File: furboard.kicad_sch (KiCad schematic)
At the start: 28 parts, among them J1 USB_C_Receptacle_USB2.0_14P, U1 RP2040, U2 NCP1117-3.3_SOT223, U3 W25Q128JVS, Y1 12 MHz

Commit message: Update the schematic data sheet thing
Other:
- title: (none) -> Furboard Devboard Schematic
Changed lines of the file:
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@@
 	(generator_version "9.0")
 	(paper "A4")
+	(title_block
+		(title "Furboard Devboard Schematic")
+	)
 	(text_box "RP2040"
 		(exclude_from_sim no)

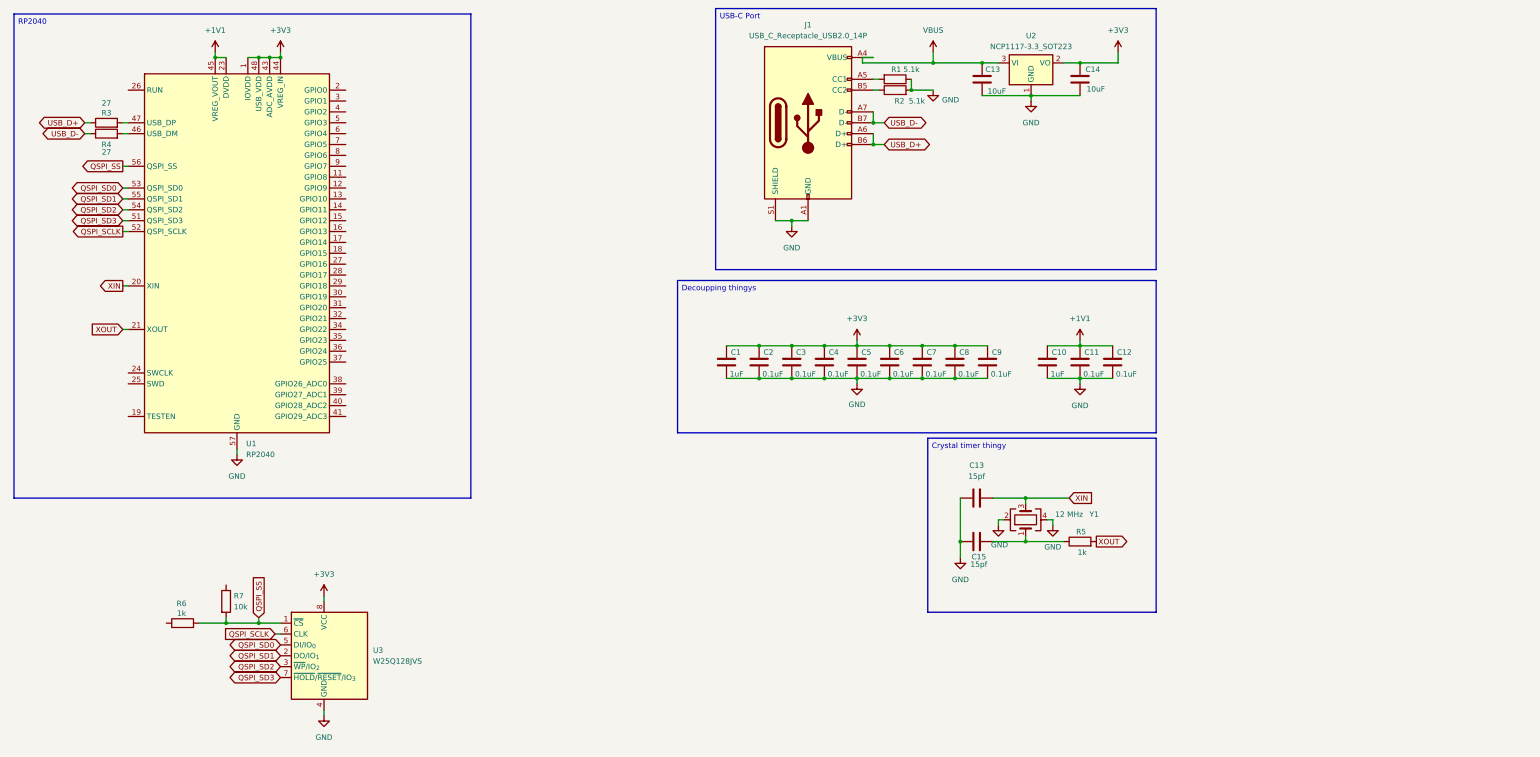
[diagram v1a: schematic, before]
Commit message: Finish schematic draft, add pinout
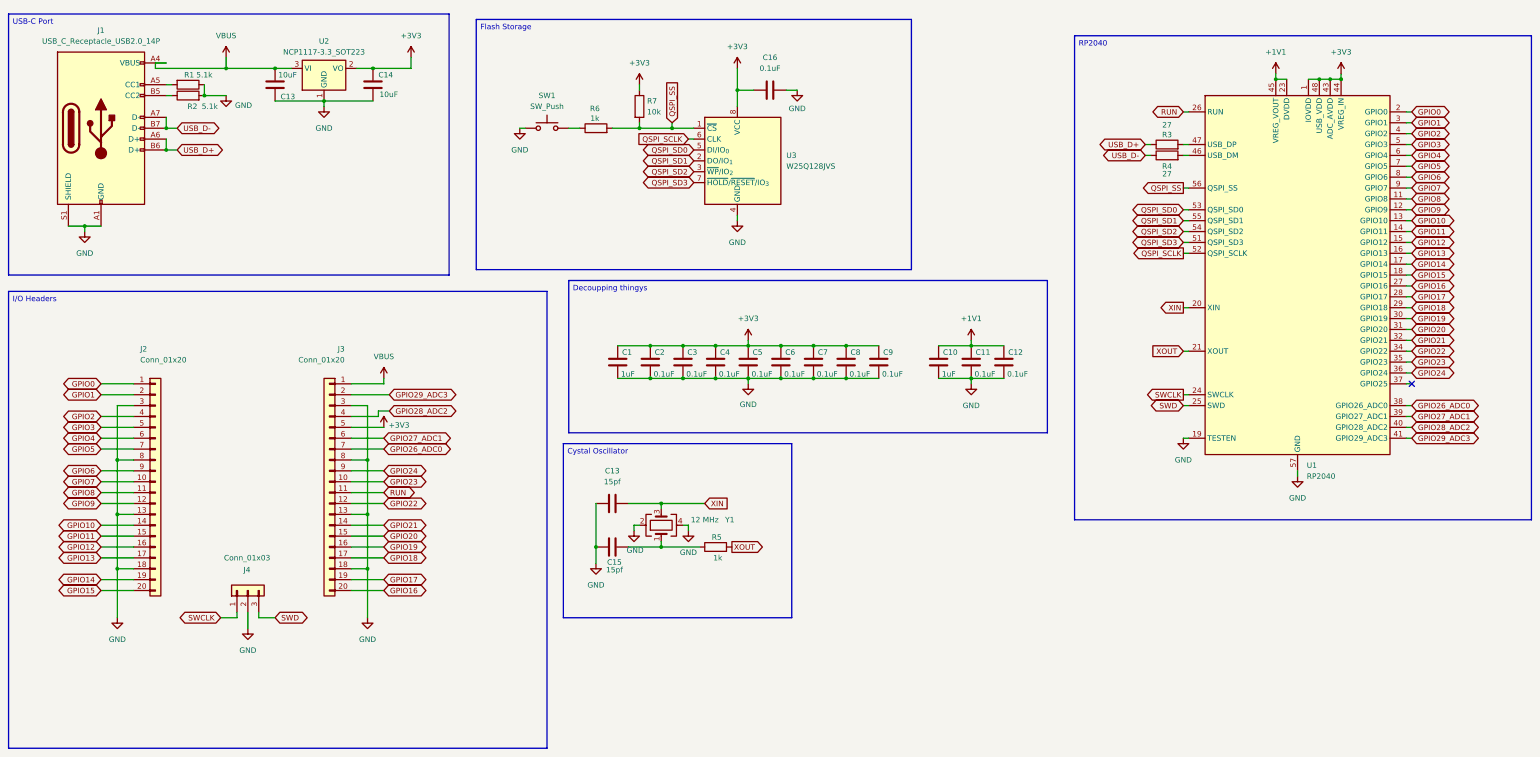
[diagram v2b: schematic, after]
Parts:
- added C16: 0.1uF, symbol Device:C
- added J2, J3: Conn_01x20, symbol Connector_Generic:Conn_01x20
- added J4: Conn_01x03, symbol Connector_Generic:Conn_01x03
- added SW1: SW_Push, symbol Switch:SW_Push
- C13: renamed from 10uF; value C13 -> 10uF
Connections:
- net +3V3: now also R7.1, C16.1, J3.5 (Pin_5)
- net GND: now also U1.19 (TESTEN), C16.2, J2.13 (Pin_13), J2.18 (Pin_18), J2.3 (Pin_3), J2.8 (Pin_8), J3.13 (Pin_13), J3.18 (Pin_18), J3.3 (Pin_3), J3.8 (Pin_8), J4.2 (Pin_2), SW1.1
- net VBUS: now also J3.1 (Pin_1)
- net at R6.1: now also SW1.2
- net GPIO8: now reaches U1.11 (GPIO8)
- net GPIO8: now also J2.11 (Pin_11)
- net GPIO9: now reaches U1.12 (GPIO9)
- net GPIO9: now also J2.12 (Pin_12)
- net GPIO10: now reaches U1.13 (GPIO10)
- net GPIO10: now also J2.14 (Pin_14)
- net GPIO11: now reaches U1.14 (GPIO11)
- net GPIO11: now also J2.15 (Pin_15)
- net GPIO12: now reaches U1.15 (GPIO12)
- net GPIO12: now also J2.16 (Pin_16)
- net GPIO13: now reaches U1.16 (GPIO13)
- net GPIO13: now also J2.17 (Pin_17)
- net GPIO14: now reaches U1.17 (GPIO14)
- net GPIO14: now also J2.19 (Pin_19)
- net GPIO15: now reaches U1.18 (GPIO15)
- net GPIO15: now also J2.20 (Pin_20)
- net GPIO0: now reaches U1.2 (GPIO0)
- net GPIO0: now also J2.1 (Pin_1)
- net SWCLK: now reaches U1.24 (SWCLK)
- net SWCLK: now also J4.1 (Pin_1)
- net SWD: now reaches U1.25 (SWD)
- net SWD: now also J4.3 (Pin_3)
- net RUN: now reaches U1.26 (RUN)
- net RUN: now also J3.11 (Pin_11)
- net GPIO16: now reaches U1.27 (GPIO16)
- net GPIO16: now also J3.20 (Pin_20)
- net GPIO17: now reaches U1.28 (GPIO17)
- net GPIO17: now also J3.19 (Pin_19)
- net GPIO18: now reaches U1.29 (GPIO18)
- net GPIO18: now also J3.17 (Pin_17)
- net GPIO1: now reaches U1.3 (GPIO1)
- net GPIO1: now also J2.2 (Pin_2)
- net GPIO19: now reaches U1.30 (GPIO19)
- net GPIO19: now also J3.16 (Pin_16)
- net GPIO20: now reaches U1.31 (GPIO20)
- net GPIO20: now also J3.15 (Pin_15)
- net GPIO21: now reaches U1.32 (GPIO21)
- net GPIO21: now also J3.14 (Pin_14)
- net GPIO22: now reaches U1.34 (GPIO22)
- net GPIO22: now also J3.12 (Pin_12)
- net GPIO23: now reaches U1.35 (GPIO23)
- net GPIO23: now also J3.10 (Pin_10)
- net GPIO24: now reaches U1.36 (GPIO24)
- net GPIO24: now also J3.9 (Pin_9)
- net GPIO26_ADC0: now reaches U1.38 (GPIO26_ADC0)
- net GPIO26_ADC0: now also J3.7 (Pin_7)
- net GPIO27_ADC1: now reaches U1.39 (GPIO27_ADC1)
- net GPIO27_ADC1: now also J3.6 (Pin_6)
- net GPIO2: now reaches U1.4 (GPIO2)
- net GPIO2: now also J2.4 (Pin_4)
- net GPIO28_ADC2: now reaches U1.40 (GPIO28_ADC2)
- net GPIO28_ADC2: now also J3.4 (Pin_4)
- net GPIO29_ADC3: now reaches U1.41 (GPIO29_ADC3)
- net GPIO29_ADC3: now also J3.2 (Pin_2)
- net GPIO3: now reaches U1.5 (GPIO3)
- net GPIO3: now also J2.5 (Pin_5)
- net GPIO4: now reaches U1.6 (GPIO4)
- net GPIO4: now also J2.6 (Pin_6)
- net GPIO5: now reaches U1.7 (GPIO5)
- net GPIO5: now also J2.7 (Pin_7)
- net GPIO6: now reaches U1.8 (GPIO6)
- net GPIO6: now also J2.9 (Pin_9)
- net GPIO7: now reaches U1.9 (GPIO7)
- net GPIO7: now also J2.10 (Pin_10)
- no-connect marks 0 -> 1
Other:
- moved on the sheet: C1, C10, C11, C12, C13, C14, C15, C2, C3, C4, C5, C6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

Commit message: Use auto-anotate to fix my issues
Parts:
- renumbered C13 to C1, C16 to C10, C6 to C11, C7 to C12, C8 to C13, C9 to C14, C10 to C15, C11 to C16, C12 to C17, C14 to C2, C13 to C3, C15 to C4, C1 to C5, C2 to C6, C3 to C7, C4 to C8, C5 to C9, J4 to J3, J3 to J4, R6 to R3, R7 to R4, R3 to R6, R4 to R7, U2 to U1, U3 to U2, U1 to U3

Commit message: Update schematic list of parts (footprint)
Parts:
- C1, C2: footprint (none) -> Capacitor_SMD:C_0201_0603Metric
- C10, C11, C12, C13, C14, C15, C16, C17, C5, C6, C7, C8, C9: footprint (none) -> Capacitor_SMD:C_0402_1005Metric
- C3, C4: value 15pf -> 33pF; footprint (none) -> Capacitor_SMD:C_0402_1005Metric
- J1: footprint (none) -> Connector_USB:USB_C_Receptacle_HRO_TYPE-C-31-M-12
- J2, J3, J4: footprint (none) -> Connector_PinHeader_2.54mm:PinHeader_1x20_P2.54mm_Vertical
- R1, R2, R3, R4, R5, R6, R7: footprint (none) -> Resistor_SMD:R_0402_1005Metric
- SW1: footprint (none) -> Button_Switch_SMD:SW_Push_SPST_NO_Alps_SKRK
- Y1: footprint (none) -> Crystal:Crystal_SMD_3225-4Pin_3.2x2.5mm
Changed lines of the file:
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@@
 			)
 		)
-		(property "Footprint" ""
+		(property "Footprint" "Capacitor_SMD:C_0402_1005Metric"
 			(at 181.3052 100.33 0)
 			(effects
@@
 			)
 		)
-		(property "Footprint" ""
+		(property "Footprint" "Capacitor_SMD:C_0402_1005Metric"
 			(at 204.1652 100.33 0)
 			(effects
@@
 			)
 		)
-		(property "Value" "15pf"
-			(at 156.718 145.034 90)
+		(property "Value" "33pF"
+			(at 157.48 145.288 90)
 			(effects
 				(font
@@
 			)
 		)
-		(property "Footprint" ""
+		(property "Footprint" "Capacitor_SMD:C_0402_1005Metric"
 			(at 160.02 138.7348 0)
 			(effects
@@
 			)
 		)
-		(property "Footprint" ""
+		(property "Footprint" "Capacitor_SMD:C_0402_1005Metric"
 			(at 240.9952 100.33 0)
 			(effects
@@
 			)
 		)
-		(property "Footprint" ""
+		(property "Footprint" "Connector_PinHeader_2.54mm:PinHeader_1x20_P2.54mm_Vertical"
 			(at 90.17 124.46 0)
 			(effects
@@
 			)
 		)
-		(property "Value" "15pf"
+		(property "Value" "33pF"
 			(at 156.21 124.46 90)
 			(effects
@@
 			)
 		)
-		(property "Footprint" ""
+		(property "Footprint" "Capacitor_SMD:C_0402_1005Metric"
 			(at 160.02 128.5748 0)
 			(effects
@@
 			)
 		)
-		(property "Footprint" ""
+		(property "Footprint" "Capacitor_SMD:C_0402_1005Metric"
 			(at 233.3752 100.33 0)
 			(effects
@@
 			)
 		)
-		(property "Footprint" ""
+		(property "Footprint" "Resistor_SMD:R_0402_1005Metric"
 			(at 285.75 47.498 90)
 			(effects
@@
 			)
 		)
-		(property "Footprint" ""
+		(property "Footprint" "Capacitor_SMD:C_0402_1005Metric"
 			(at 188.9252 100.33 0)
 			(effects
@@
 			)
 		)
-		(property "Footprint" ""
+		(property "Footprint" "Capacitor_SMD:C_0402_1005Metric"
 			(at 196.5452 100.33 0)
 			(effects
@@
 			)
 		)
-		(property "Footprint" ""
+		(property "Footprint" "Resistor_SMD:R_0402_1005Metric"
 			(at 180.34 141.478 90)
 			(effects
@@
 			)
 		)
-		(property "Footprint" ""
+		(property "Footprint" "Capacitor_SMD:C_0402_1005Metric"
 			(at 248.6152 100.33 0)
 			(effects
@@
 			)
 		)
-		(property "Footprint" ""
+		(property "Footprint" "Capacitor_SMD:C_0402_1005Metric"
 			(at 219.4052 100.33 0)
 			(effects
@@
 			)
 		)
-		(property "Footprint" ""
+		(property "Footprint" "Button_Switch_SMD:SW_Push_SPST_NO_Alps_SKRK"
 			(at 140.97 36.83 0)
 			(effects
@@
 			)
 		)
-		(property "Footprint" ""
+		(property "Footprint" "Capacitor_SMD:C_0402_1005Metric"
 			(at 211.7852 100.33 0)
 			(effects
@@
 			)
 		)
-		(property "Footprint" ""
+		(property "Footprint" "Capacitor_SMD:C_0201_0603Metric"
 			(at 101.2952 35.56 0)
 			(effects
@@
 			)
 		)
-		(property "Footprint" ""
+		(property "Footprint" "Crystal:Crystal_SMD_3225-4Pin_3.2x2.5mm"
 			(at 167.64 134.62 0)
 			(effects
@@
 			)
 		)
-		(property "Footprint" ""
+		(property "Footprint" "Resistor_SMD:R_0402_1005Metric"
 			(at 160.782 36.83 90)
 			(effects
@@
 			)
 		)
-		(property "Footprint" ""
+		(property "Footprint" "Capacitor_SMD:C_0402_1005Metric"
 			(at 196.85 32.0548 0)
 			(effects
@@
 			)
 		)
-		(property "Footprint" ""
+		(property "Footprint" "Connector_USB:USB_C_Receptacle_HRO_TYPE-C-31-M-12"
 			(at 40.64 41.91 0)
 			(effects
@@
 			)
 		)
-		(property "Footprint" ""
+		(property "Footprint" "Connector_PinHeader_2.54mm:PinHeader_1x20_P2.54mm_Vertical"
 			(at 49.53 124.46 0)
 			(effects
@@
 			)
 		)
-		(property "Footprint" ""
+		(property "Footprint" "Capacitor_SMD:C_0402_1005Metric"
 			(at 173.6852 100.33 0)
 			(effects
@@
 			)
 		)
-		(property "Footprint" ""
+		(property "Footprint" "Resistor_SMD:R_0402_1005Metric"
 			(at 57.15 29.972 90)
 			(effects
@@
 			)
 		)
-		(property "Footprint" ""
+		(property "Footprint" "Connector_PinHeader_2.54mm:PinHeader_1x20_P2.54mm_Vertical"
 			(at 71.12 149.86 0)
 			(effects
@@
 			)
 		)
-		(property "Footprint" ""
+		(property "Footprint" "Capacitor_SMD:C_0201_0603Metric"
 			(at 78.4352 35.56 0)
 			(effects
@@
 			)
 		)
-		(property "Footprint" ""
+		(property "Footprint" "Resistor_SMD:R_0402_1005Metric"
 			(at 152.4 43.688 90)
 			(effects
@@
 			)
 		)
-		(property "Footprint" ""
+		(property "Footprint" "Capacitor_SMD:C_0402_1005Metric"
 			(at 158.4452 100.33 0)
 			(effects
@@
 			)
 		)
-		(property "Footprint" ""
+		(property "Footprint" "Resistor_SMD:R_0402_1005Metric"
 			(at 285.75 50.038 90)
 			(effects
@@
 			)
 		)
-		(property "Footprint" ""
+		(property "Footprint" "Resistor_SMD:R_0402_1005Metric"
 			(at 57.15 36.068 90)
 			(effects
@@
 			)
 		)
-		(property "Footprint" ""
+		(property "Footprint" "Capacitor_SMD:C_0402_1005Metric"
 			(at 166.0652 100.33 0)
 			(effects

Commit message: Start working on the PCB, add shape, pins, and RP2040
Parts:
- J3: footprint Connector_PinHeader_2.54mm:PinHeader_1x20_P2.54mm_Vertical -> Connector_PinHeader_2.54mm:PinHeader_1x03_P2.54mm_Vertical
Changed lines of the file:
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@@
 			)
 		)
-		(property "Footprint" "Connector_PinHeader_2.54mm:PinHeader_1x20_P2.54mm_Vertical"
+		(property "Footprint" "Connector_PinHeader_2.54mm:PinHeader_1x03_P2.54mm_Vertical"
 			(at 71.12 149.86 0)
 			(effects
